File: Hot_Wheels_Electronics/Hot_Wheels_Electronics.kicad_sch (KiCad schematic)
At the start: 15 parts, among them J1 motor_output, M1 motor_driver: DRV8833PW, SW1 main_switch, U1 esp32-wemos-d1-mini, U3 BMI160, U4 QITN BEC

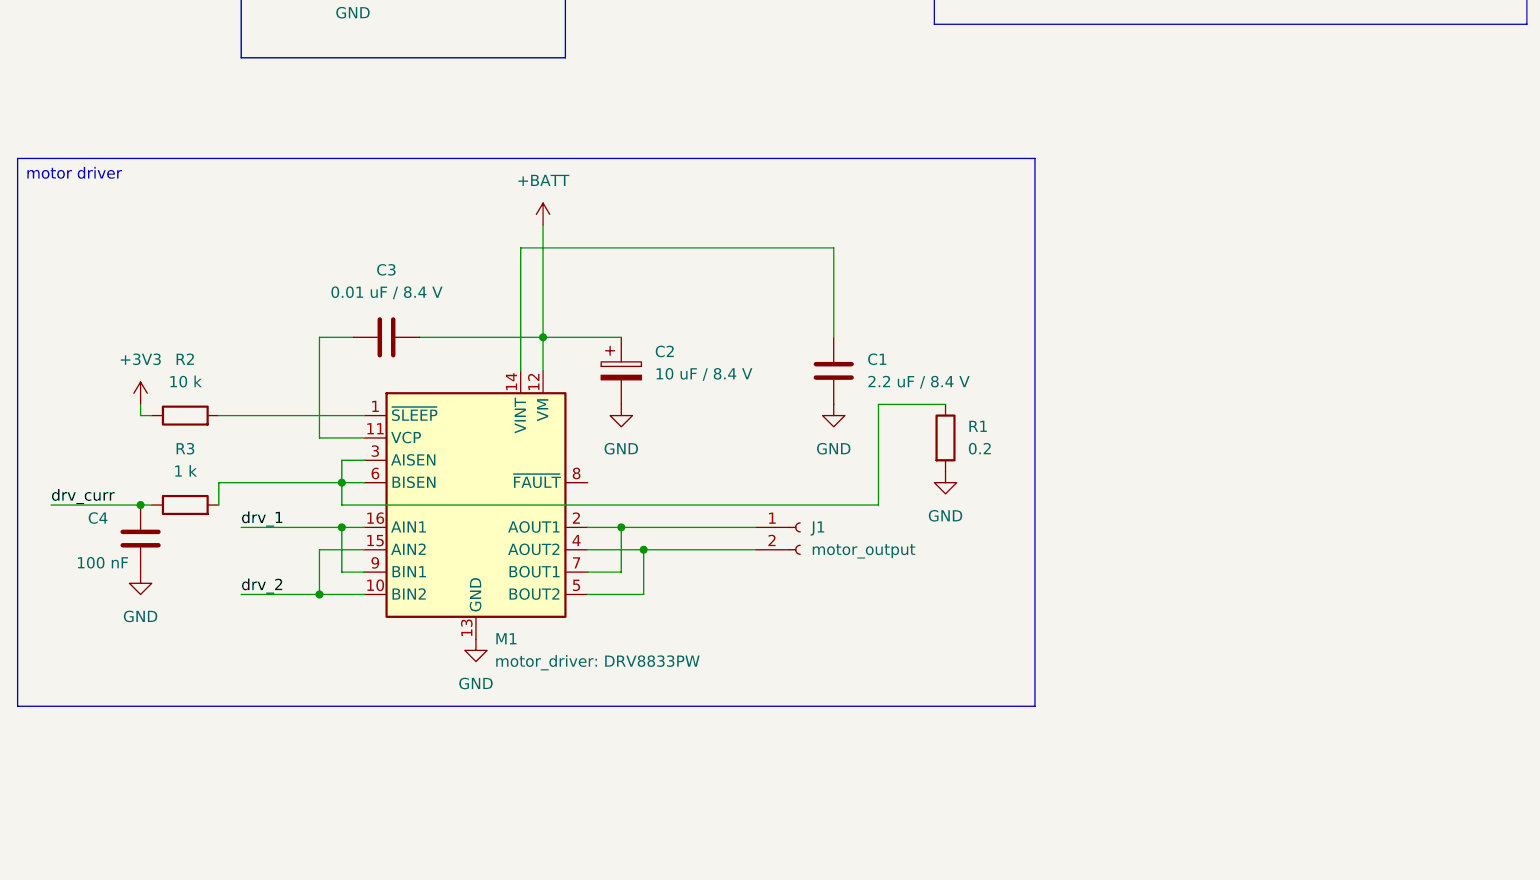
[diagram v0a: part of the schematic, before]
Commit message: feat: enabled two independent motor drivers
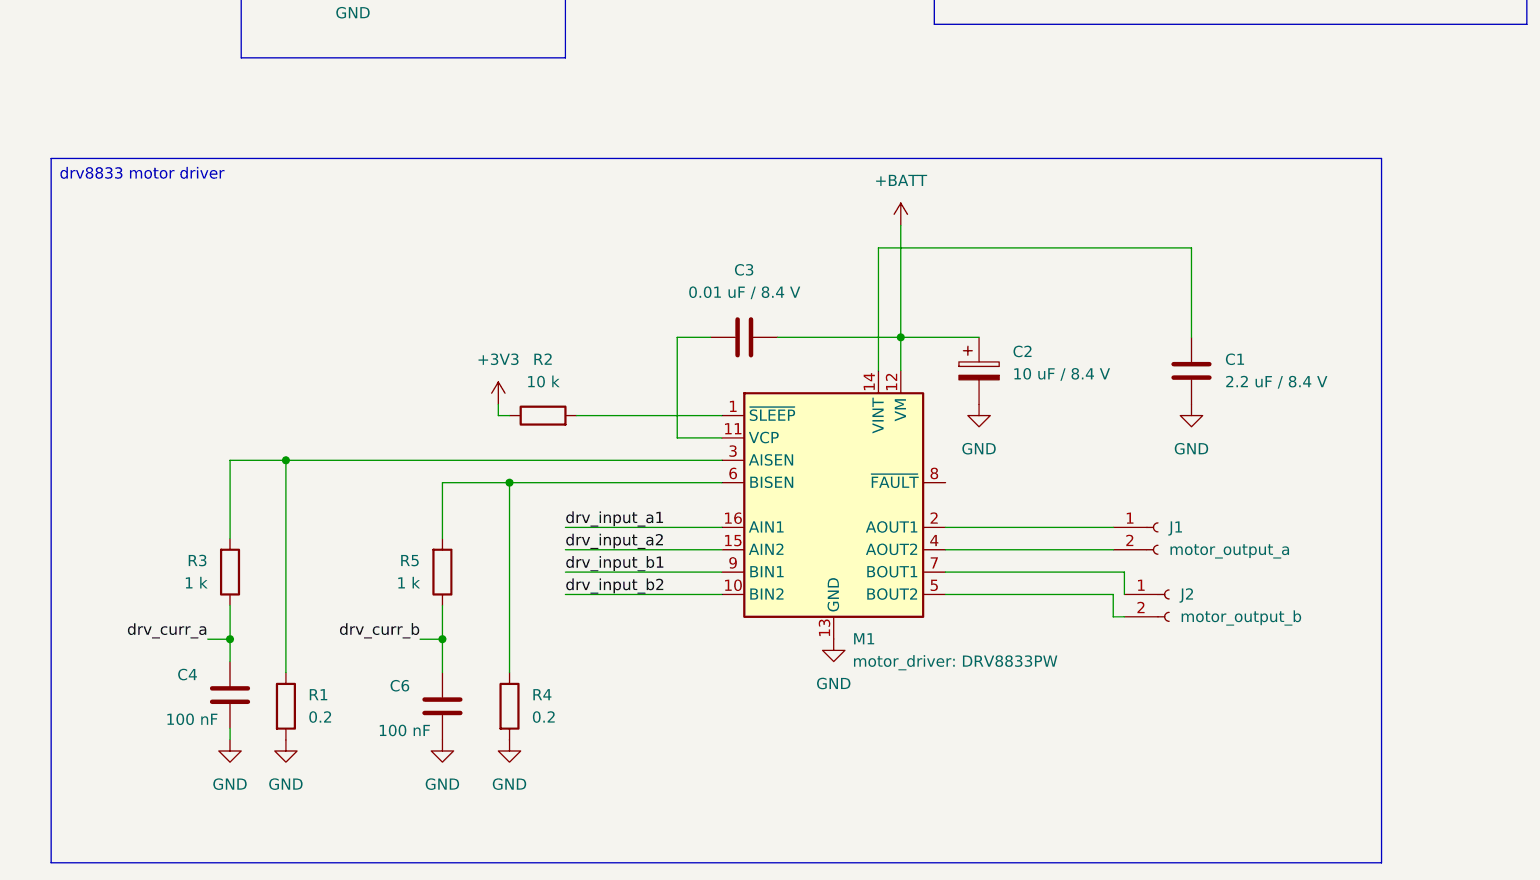
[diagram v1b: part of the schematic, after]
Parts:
- added C6: 100 nF, symbol Device:C
- added J2: motor_output_b, Connector_JST:JST_PH_S2B-PH-K_1x02_P2.00mm_Horizontal, symbol Connector:Conn_01x02_Socket
- added R4: 0.2, symbol Device:R
- added R5: 1 k, symbol Device:R
- J1: value motor_output -> motor_output_a
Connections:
- net GND: now also C6.2, R4.2
- net drv_1: no longer M1.16 (AIN1), M1.9 (BIN1)
- net drv_2: no longer M1.10 (BIN2), M1.15 (AIN2)
- net drv_curr: no longer C4.1, R3.1
- net at J1.1 (Pin_1), M1.2 (AOUT1): no longer M1.7 (BOUT1)
- net at M1.3 (AISEN), R1.1, R3.2: no longer M1.6 (BISEN)
- net at J1.2 (Pin_2), M1.4 (AOUT2): no longer M1.5 (BOUT2)
- new net: J2.1 (Pin_1), M1.7 (BOUT1)
- new net: J2.2 (Pin_2), M1.5 (BOUT2)
- new net: M1.6 (BISEN), R4.1, R5.2
- new net drv_curr_a: C4.1, R3.1
- new net drv_curr_b: C6.1, R5.1
- new net drv_input_a1: M1.16 (AIN1)
- new net drv_input_a2: M1.15 (AIN2)
- new net drv_input_b1: M1.9 (BIN1)
- new net drv_input_b2: M1.10 (BIN2)
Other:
- moved on the sheet: C1, C2, C3, C4, J1, M1, R1, R2, R3

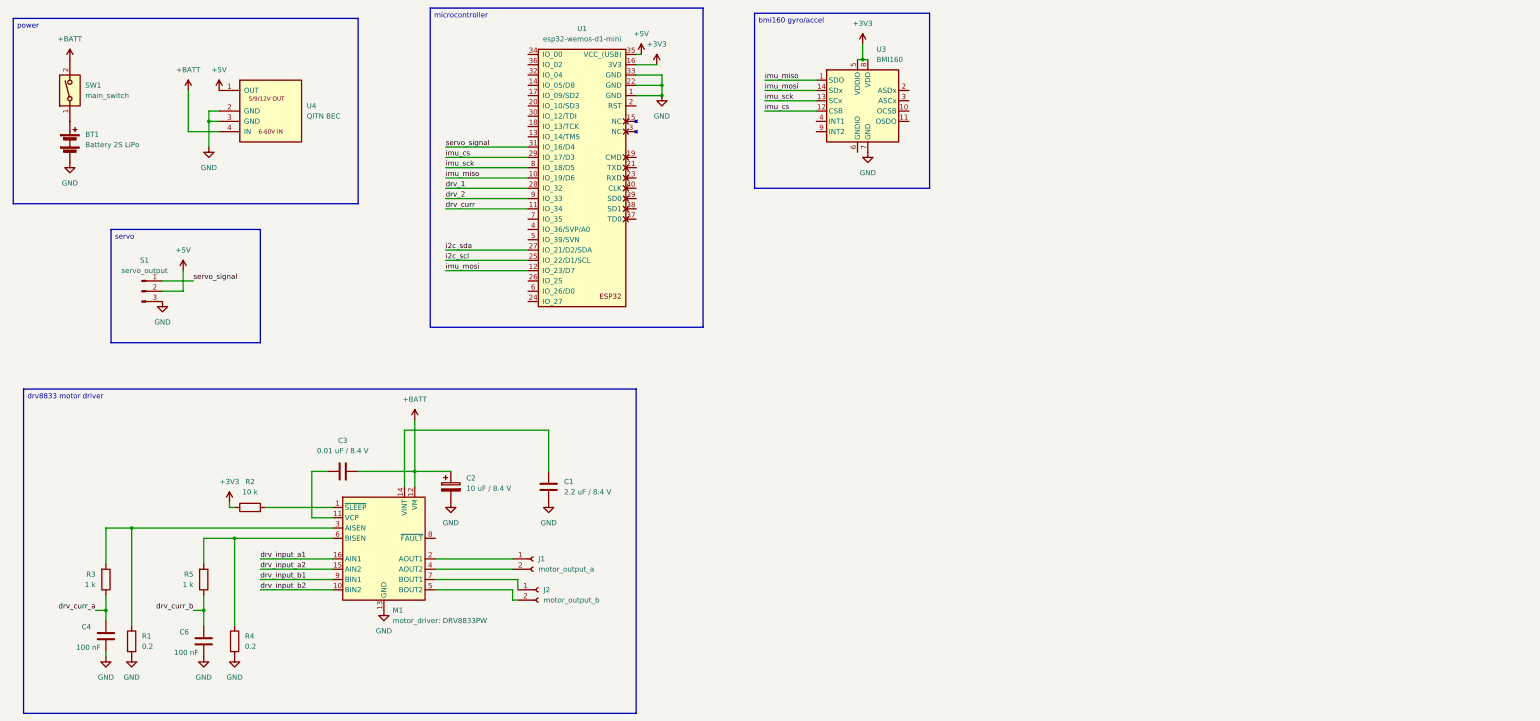
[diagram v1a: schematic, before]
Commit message: migrated to bare castellated module and used safe gpio pins
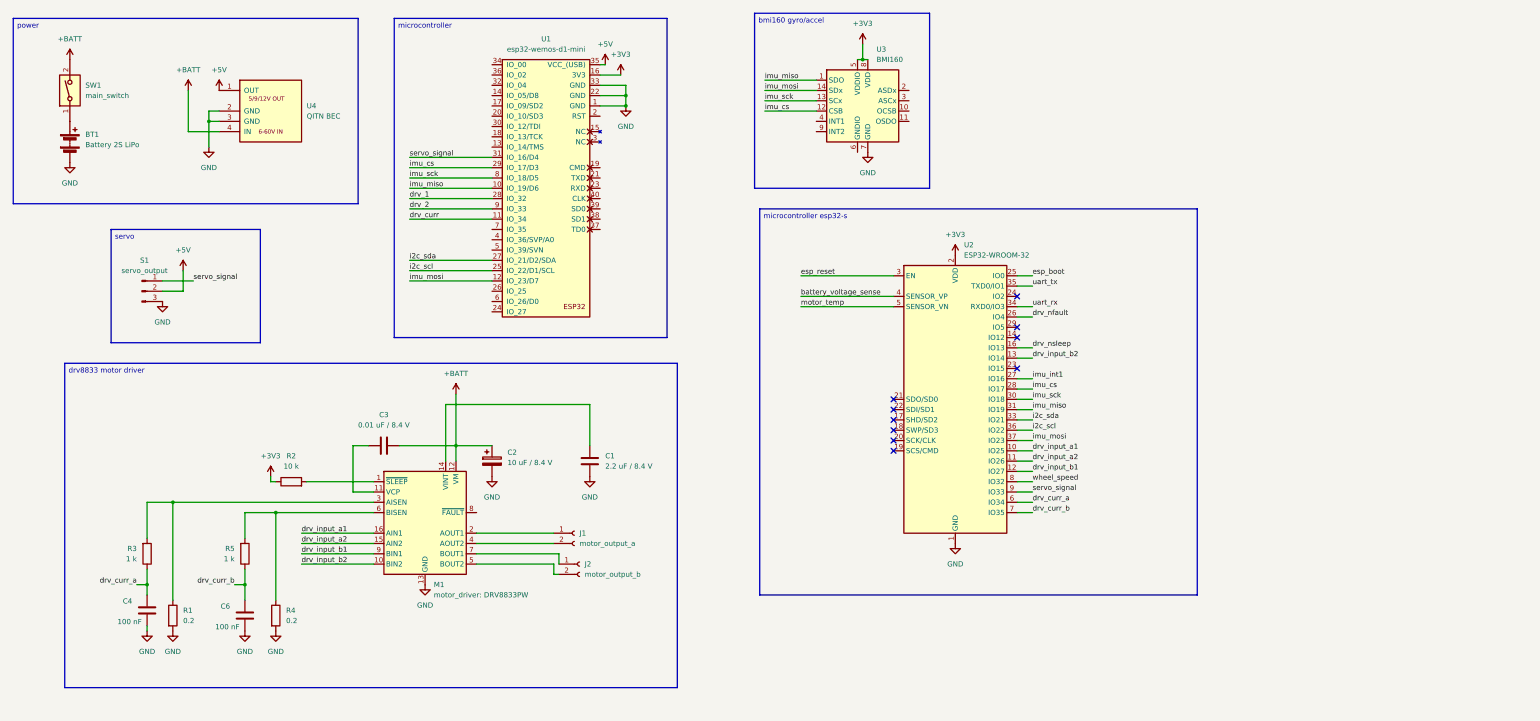
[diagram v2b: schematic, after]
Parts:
- added U2: ESP32-WROOM-32, RF_Module:ESP32-WROOM-32, symbol RF_Module:ESP32-WROOM-32
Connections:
- net +3V3: now also U2.2 (VDD)
- net GND: now also U2.1 (GND), U2.15 (GND), U2.38 (GND), U2.39 (GND)
- net drv_curr_a: now also U2.6 (IO34)
- net drv_curr_b: now also U2.7 (IO35)
- net drv_input_a1: now also U2.10 (IO25)
- net drv_input_a2: now also U2.11 (IO26)
- net drv_input_b1: now also U2.12 (IO27)
- net drv_input_b2: now also U2.13 (IO14)
- net i2c_scl: now also U2.36 (IO22)
- net i2c_sda: now also U2.33 (IO21)
- net imu_cs: now also U2.28 (IO17)
- net imu_miso: now also U2.31 (IO19)
- net imu_mosi: now also U2.37 (IO23)
- net imu_sck: now also U2.30 (IO18)
- net servo_signal: now also U2.9 (IO33)
- new net battery_voltage_sense: U2.4 (SENSOR_VP)
- new net drv_nfault: U2.26 (IO4)
- new net drv_nsleep: U2.16 (IO13)
- new net esp_boot: U2.25 (IO0)
- new net esp_reset: U2.3 (EN)
- new net imu_int1: U2.27 (IO16)
- new net motor_temp: U2.5 (SENSOR_VN)
- new net uart_rx: U2.34 (RXD0/IO3)
- new net uart_tx: U2.35 (TXD0/IO1)
- new net wheel_speed: U2.8 (IO32)
- no-connect marks 0 -> 10
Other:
- moved on the sheet: C1, C2, C3, C4, C6, J1, J2, M1, R1, R2, R3, R4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

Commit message: worked on programmer
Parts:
- added J3: Conn_02x05_Socket, Connector_RJ:RJ45_Abracon_ARJP11A-MA_Horizontal, symbol Connector_Generic:Conn_02x05_Counter_Clockwise
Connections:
- net GND: now also J3.4 (Pin_4), J3.5 (Pin_5)
- net uart_rx: now also J3.8 (Pin_8)
- net uart_tx: now also J3.7 (Pin_7)
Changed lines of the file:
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@@
 		)
 	)
+	(text_box "programming interface"
+		(exclude_from_sim no)
+		(at 326.39 63.5 0)
+		(size 68.58 76.2)
+		(margins 0.9525 0.9525 0.9525 0.9525)
+		(stroke
+			(width 0)
+			(type solid)
+		)
+		(fill
+			(type none)
+		)
+		(effects
+			(font
+				(size 1.27 1.27)
+			)
+			(justify left top)
+		)
+	)
 	(text_box "power"
 		(exclude_from_sim no)
@@
 	)
 	(junction
+		(at 358.14 100.33)
+		(diameter 0)
+		(color 0 0 0 0)
+	)
+	(junction
 		(at 129.54 121.92)
 		(diameter 0)
@@
 	(wire
 		(pts
+			(xy 358.14 97.79) (xy 358.14 100.33)
+		)
+		(stroke
+			(width 0)
+			(type default)
+		)
+	)
+	(wire
+		(pts
 			(xy 171.45 33.02) (xy 171.45 35.56)
 		)
@@
 		)
 	)
+	(label "uart_rx"
+		(at 370.84 95.25 0)
+		(effects
+			(font
+				(size 1.27 1.27)
+			)
+			(justify left bottom)
+		)
+	)
 	(label "uart_tx"
 		(at 271.78 82.55 0)
@@
 		)
 	)
+	(label "uart_tx"
+		(at 370.84 97.79 0)
+		(effects
+			(font
+				(size 1.27 1.27)
+			)
+			(justify left bottom)
+		)
+	)
 	(label "drv_1"
 		(at 118.11 60.96 0)
@@
 		)
 	)
+	(label "esp_reset"
+		(at 347.98 80.01 0)
+		(effects
+			(font
+				(size 1.27 1.27)
+			)
+			(justify left bottom)
+		)
+	)
 	(label "i2c_sda"
 		(at 271.78 115.57 0)
@@
 		)
 	)
+	(label "esp_boot"
+		(at 367.03 77.47 0)
+		(effects
+			(font
+				(size 1.27 1.27)
+			)
+			(justify left bottom)
+		)
+	)
 	(label "servo_signal"
 		(at 271.78 133.35 0)
@@
 	)
 	(symbol
+		(lib_id "Connector_Generic:Conn_02x05_Counter_Clockwise")
+		(at 363.22 95.25 0)
+		(unit 1)
+		(body_style 1)
+		(exclude_from_sim no)
+		(in_bom yes)
+		(on_board yes)
+		(in_pos_files yes)
+		(dnp no)
+		(property "Reference" "J3"
+			(at 364.49 104.902 0)
+			(show_name no)
+			(do_not_autoplace no)
+			(effects
+				(font
+					(size 1.27 1.27)
+				)
+				(justify left)
+			)
+		)
+		(property "Value" "Conn_02x05_Socket"
+			(at 364.236 103.124 0)
+			(show_name no)
+			(do_not_autoplace no)
+			(effects
+				(font
+					(size 1.27 1.27)
+				)
+				(justify left)
+			)
+		)
+		(property "Footprint" "Connector_RJ:RJ45_Abracon_ARJP11A-MA_Horizontal"
+			(at 363.22 95.25 0)
+			(hide yes)
+			(show_name no)
+			(do_not_autoplace no)
+			(effects
+				(font
+					(size 1.27 1.27)
+				)
+			)
+		)
+		(property "Datasheet" ""
+			(at 363.22 95.25 0)
+			(hide yes)
+			(show_name no)
+			(do_not_autoplace no)
+			(effects
+				(font
+					(size 1.27 1.27)
+				)
+			)
+		)
+		(property "Description" "Generic connector, double row, 02x05, counter clockwise pin numbering scheme (similar to DIP package numbering), script generated (kicad-library-utils/schlib/autogen/connector/)"
+			(at 363.22 95.25 0)
+			(hide yes)
+			(show_name no)
+			(do_not_autoplace no)
+			(effects
+				(font
+					(size 1.27 1.27)
+				)
+			)
+		)
+		(pin "3"
+		)
+		(pin "2"
+		)
+		(pin "4"
+		)
+		(pin "5"
+		)
+		(pin "1"
+		)
+		(pin "7"
+		)
+		(pin "10"
+		)
+		(pin "6"
+		)
+		(pin "8"
+		)
+		(pin "9"
+		)
+		(instances
+			(project "Hot_Wheels_Electronics"
+				(path "/753fef37-370a-4893-8adb-358cd7fc1669"
+					(reference "J3")
+					(unit 1)
+				)
+			)
+		)
+	)
+	(symbol
 		(lib_id "esp32-wemos-d1-mini:esp32-wemos-d1-mini")
 		(at 151.13 25.4 0)
@@
 					(unit 1)
 				)
+			)
+		)
+	)
+	(symbol
+		(lib_id "power:GND")
+		(at 358.14 100.33 0)
+		(unit 1)
+		(body_style 1)
+		(exclude_from_sim no)
+		(in_bom yes)
+		(on_board yes)
+		(in_pos_files yes)
+		(dnp no)
+		(fields_autoplaced yes)
+		(property "Reference" "#PWR024"
+			(at 358.14 106.68 0)
+			(hide yes)
+			(show_name no)
+			(do_not_autoplace no)
+			(effects
+				(font
+					(size 1.27 1.27)
+				)
+			)
+		)
+		(property "Value" "GND"
+			(at 358.14 105.41 0)
+			(show_name no)
+			(do_not_autoplace no)
+			(effects
+				(font
+					(size 1.27 1.27)
+				)
+			)
+		)
+		(property "Footprint" ""
+			(at 358.14 100.33 0)
+			(hide yes)
+			(show_name no)
+			(do_not_autoplace no)
+			(effects
+				(font
+					(size 1.27 1.27)
+				)
+			)
+		)
+		(property "Datasheet" ""
+			(at 358.14 100.33 0)
+			(hide yes)
+			(show_name no)
+			(do_not_autoplace no)
+			(effects
+				(font
+					(size 1.27 1.27)
+				)
+			)
+		)
+		(property "Description" "Power symbol creates a global label with name \"GND\" , ground"
+			(at 358.14 100.33 0)
+			(hide yes)
+			(show_name no)
+			(do_not_autoplace no)
+			(effects
+				(font
+					(size 1.27 1.27)
+				)
+			)
+		)
+		(pin "1"
+		)
+		(instances
+			(project "Hot_Wheels_Electronics"
+				(path "/753fef37-370a-4893-8adb-358cd7fc1669"
+					(reference "#PWR024")
+					(unit 1)
+				)
